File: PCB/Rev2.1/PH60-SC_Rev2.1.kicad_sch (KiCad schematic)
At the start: 44 parts, among them J1 USB_C_Receptacle_USB2.0_14P, J2 Conn_01x02_Pin, J3 Conn_01x02_Pin, U1 nRF52840, X1 32.768kHz, X2 Crystal_Generic

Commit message: 扇出sc7a210h开发用引脚
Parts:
- added J4: Conn_01x08_Pin, Connector_PinSocket_2.54mm:PinSocket_1x08_P2.54mm_Vertical, symbol Connector:Conn_01x08_Pin
- added J5: Conn_01x03_Pin, Connector_PinSocket_2.54mm:PinSocket_1x03_P2.54mm_Vertical, symbol Connector:Conn_01x03_Pin
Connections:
- net GND: now also J4.8 (Pin_8)
- net VDD_NRF: now also J5.3 (Pin_3)
- net INT2: now reaches U1.A14 (P1.15)
- net INT2: now also J4.6 (Pin_6)
- net INT1: now reaches U1.A16 (P1.13)
- net INT1: now also J4.5 (Pin_5)
- net CS: now reaches U1.A20 (P1.10)
- net CS: now also J4.1 (Pin_1)
- net SDO/SA0: now reaches U1.B15 (P1.14)
- net SDO/SA0: now also J4.4 (Pin_4)
- net SDA/SDO/SDI: now reaches U1.B17 (P1.12)
- net SDA/SDO/SDI: now also J4.3 (Pin_3)
- net SCL/SPC: now reaches U1.B19 (P1.11)
- net SCL/SPC: now also J4.2 (Pin_2)
- net GPIO_VDD_OUT: now reaches U1.B9 (AIN6/P0.30)
- net GPIO_VDD_OUT: now also J5.1 (Pin_1)
- new net IMU_VCC: J4.7 (Pin_7), J5.2 (Pin_2)
- no-connect marks 24 -> 17
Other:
- moved on the sheet: J2, J3

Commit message: 丝印添加
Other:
- moved on the sheet: J5
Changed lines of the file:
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@@
 	)
 	(label "VDD_NRF"
-		(at 300.99 175.26 0)
+		(at 295.91 182.88 0)
 		(effects
 			(font
@@
 	)
 	(label "IMU_VCC"
-		(at 300.99 172.72 0)
+		(at 295.91 180.34 0)
 		(effects
 			(font
@@
 	)
 	(label "GPIO_VDD_OUT"
-		(at 300.99 170.18 0)
+		(at 295.91 177.8 0)
 		(effects
 			(font
@@
 	(symbol
 		(lib_id "Connector:Conn_01x03_Pin")
-		(at 295.91 172.72 0)
+		(at 290.83 180.34 0)
 		(unit 1)
 		(body_style 1)
@@
 		(fields_autoplaced yes)
 		(property "Reference" "J5"
-			(at 296.545 165.1 0)
+			(at 291.465 172.72 0)
 			(show_name no)
 			(do_not_autoplace no)
@@
 		)
 		(property "Value" "Conn_01x03_Pin"
-			(at 296.545 167.64 0)
+			(at 291.465 175.26 0)
 			(show_name no)
 			(do_not_autoplace no)
@@
 		)
 		(property "Footprint" "Connector_PinSocket_2.54mm:PinSocket_1x03_P2.54mm_Vertical"
-			(at 295.91 172.72 0)
+			(at 290.83 180.34 0)
 			(hide yes)
 			(show_name no)
@@
 		)
 		(property "Datasheet" ""
-			(at 295.91 172.72 0)
+			(at 290.83 180.34 0)
 			(hide yes)
 			(show_name no)
@@
 		)
 		(property "Description" "Generic connector, single row, 01x03, script generated"
-			(at 295.91 172.72 0)
-			(hide yes)
-			(show_name no)
+			(at 290.83 180.34 0)
+			(hide yes)
+			(show_name no)

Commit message: 调整天线封装与相关外围元件bom，c27dnf，0欧电阻换1.2nh电感
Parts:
- removed R3: 0R, Capacitor_SMD:C_0402_1005Metric, symbol Device:R
- added L5: 1.2 nH, Inductor_SMD:L_0402_1005Metric, symbol Device:L_Small
- C10: value 0.5p -> 2.8p
- C27: now left out of the parts list
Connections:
- net at AE1.1 (A), C27.2: now also L5.1
- net at C10.2, L2.1: now also L5.2
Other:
- note added: "C27（DNF）"
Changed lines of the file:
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@@
 		)
 	)
+	(text "C27（DNF）"
+		(exclude_from_sim no)
+		(at 139.954 109.474 0)
+		(effects
+			(font
+				(size 1.27 1.27)
+			)
+		)
+	)
 	(text "ESD"
 		(exclude_from_sim no)
@@
 	(wire
 		(pts
+			(xy 158.75 104.14) (xy 163.83 104.14)
+		)
+		(stroke
+			(width 0)
+			(type default)
+		)
+	)
+	(wire
+		(pts
 			(xy 181.61 193.04) (xy 190.5 193.04)
 		)
@@
 	(wire
 		(pts
-			(xy 160.02 104.14) (xy 163.83 104.14)
-		)
-		(stroke
-			(width 0)
-			(type default)
-		)
-	)
-	(wire
-		(pts
 			(xy 275.59 60.96) (xy 285.75 60.96)
 		)
@@
 	(wire
 		(pts
-			(xy 147.32 104.14) (xy 152.4 104.14)
+			(xy 147.32 104.14) (xy 153.67 104.14)
 		)
 		(stroke
@@
 	)
 	(symbol
-		(lib_id "Device:R")
-		(at 156.21 104.14 90)
-		(unit 1)
-		(body_style 1)
-		(exclude_from_sim no)
-		(in_bom yes)
-		(on_board yes)
-		(in_pos_files yes)
-		(dnp no)
-		(fields_autoplaced yes)
-		(property "Reference" "R3"
-			(at 156.21 97.79 90)
-			(show_name no)
-			(do_not_autoplace no)
-			(effects
-				(font
-					(size 1.27 1.27)
-				)
-			)
-		)
-		(property "Value" "0R"
-			(at 156.21 100.33 90)
-			(show_name no)
-			(do_not_autoplace no)
-			(effects
-				(font
-					(size 1.27 1.27)
-				)
-			)
-		)
-		(property "Footprint" "Capacitor_SMD:C_0402_1005Metric"
-			(at 156.21 105.918 90)
-			(hide yes)
-			(show_name no)
-			(do_not_autoplace no)
-			(effects
-				(font
-					(size 1.27 1.27)
-				)
-			)
-		)
-		(property "Datasheet" ""
-			(at 156.21 104.14 0)
-			(hide yes)
-			(show_name no)
-			(do_not_autoplace no)
-			(effects
-				(font
-					(size 1.27 1.27)
-				)
-			)
-		)
-		(property "Description" "Resistor"
-			(at 156.21 104.14 0)
-			(hide yes)
-			(show_name no)
-			(do_not_autoplace no)
-			(effects
-				(font
-					(size 1.27 1.27)
-				)
-			)
-		)
-		(pin "2"
-		)
-		(pin "1"
-		)
-		(instances
-			(project "PH60-SC_Rev2.1"
-				(path "/dca0f898-8fdb-4522-a51d-f4f4238906e7"
-					(reference "R3")
-					(unit 1)
-				)
-			)
-		)
-	)
-	(symbol
 		(lib_id "Device:C_Small")
 		(at 139.7 54.61 0)
@@
 			)
 		)
-		(property "Value" "0.5p"
+		(property "Value" "2.8p"
 			(at 166.37 109.2135 0)
 			(show_name no)
@@
 		(body_style 1)
 		(exclude_from_sim no)
-		(in_bom yes)
+		(in_bom no)
 		(on_board yes)
 		(in_pos_files yes)
@@
 					(unit 1)
 				)
+			)
+		)
+	)
+	(symbol
+		(lib_id "Device:L_Small")
+		(at 156.21 104.14 90)
+		(unit 1)
+		(body_style 1)
+		(exclude_from_sim no)
+		(in_bom yes)
+		(on_board yes)
+		(in_pos_files yes)
+		(dnp no)
+		(fields_autoplaced yes)
+		(property "Reference" "L5"
+			(at 156.21 99.06 90)
+			(show_name no)
+			(do_not_autoplace no)
+			(effects
+				(font
+					(size 1.27 1.27)
+				)
+			)
+		)
+		(property "Value" "1.2 nH"
+			(at 156.21 101.6 90)
+			(show_name no)
+			(do_not_autoplace no)
+			(effects
+				(font
+					(size 1.27 1.27)
+				)
+			)
+		)
+		(property "Footprint" "Inductor_SMD:L_0402_1005Metric"
+			(at 156.21 104.14 0)
+			(hide yes)
+			(show_name no)
+			(do_not_autoplace no)
+			(effects
+				(font
+					(size 1.27 1.27)
+				)
+			)
+		)
+		(property "Datasheet" ""
+			(at 156.21 104.14 0)
+			(hide yes)
+			(show_name no)
+			(do_not_autoplace no)
+			(effects
+				(font
+					(size 1.27 1.27)
+				)
+			)
+		)
+		(property "Description" "Inductor, small symbol"
+			(at 156.21 104.14 0)
+			(hide yes)
+			(show_name no)
+			(do_not_autoplace no)
+			(effects
+				(font
+					(size 1.27 1.27)
+				)
+			)
+		)
+		(pin "2"
+		)
+		(pin "1"
+		)
+		(instances
+			(project "PH60-SC_Rev2.1"
+				(path "/dca0f898-8fdb-4522-a51d-f4f4238906e7"
+					(reference "L5")
+					(unit 1)
+				)

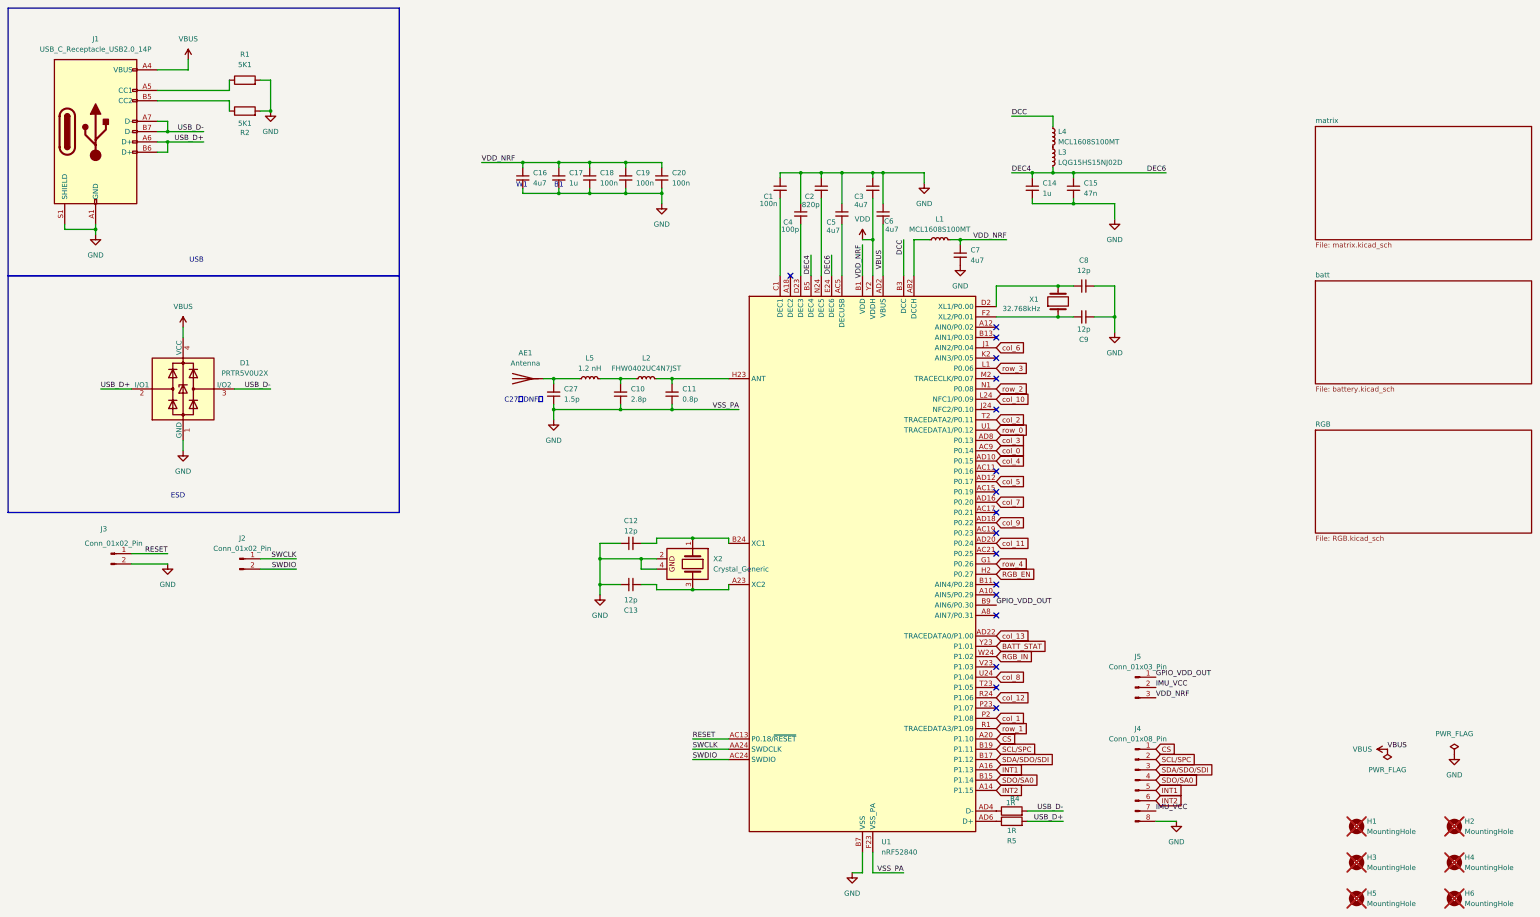
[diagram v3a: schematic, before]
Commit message: 布局调整，rgb，轴座调整，注意二极管位置为手动校准
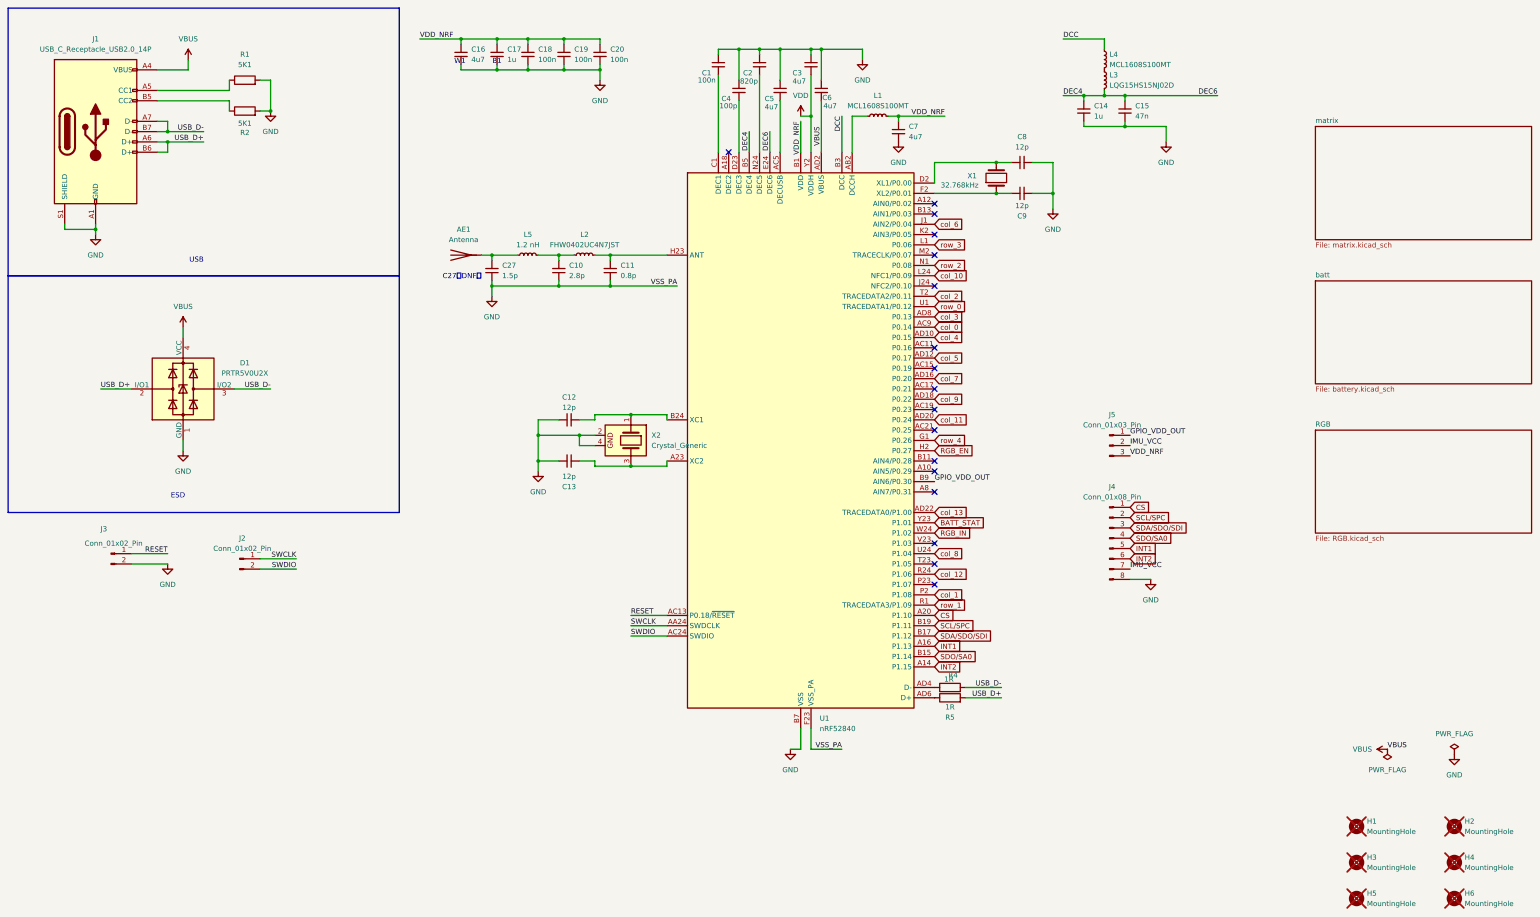
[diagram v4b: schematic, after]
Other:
- moved on the sheet: AE1, C1, C10, C11, C12, C13, C14, C15, C16, C17, C18, C19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

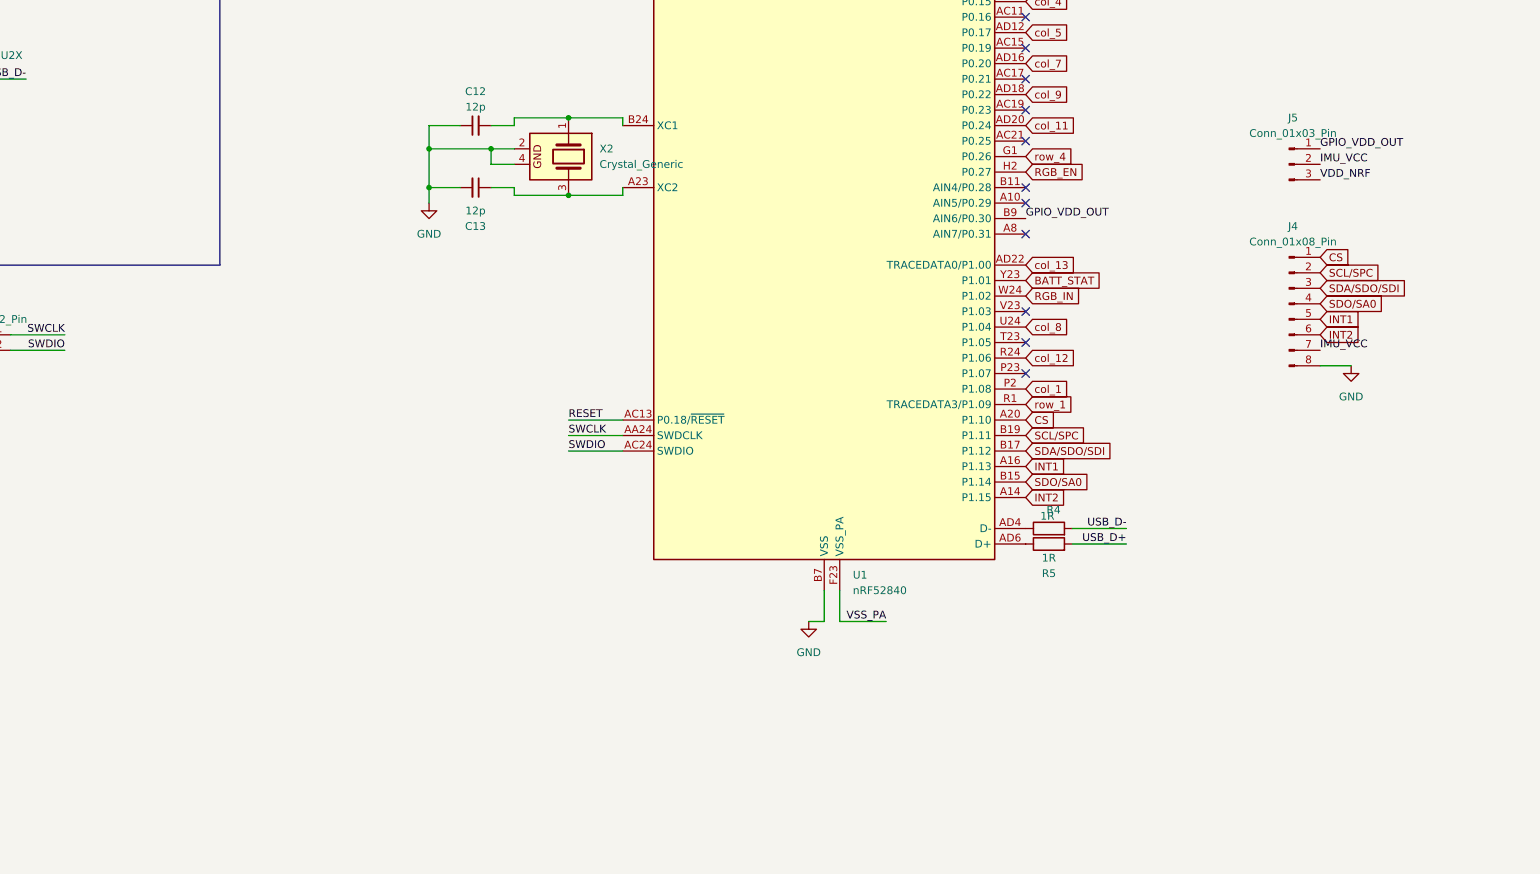
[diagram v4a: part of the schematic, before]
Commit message: 原理图添加LIS2DH12
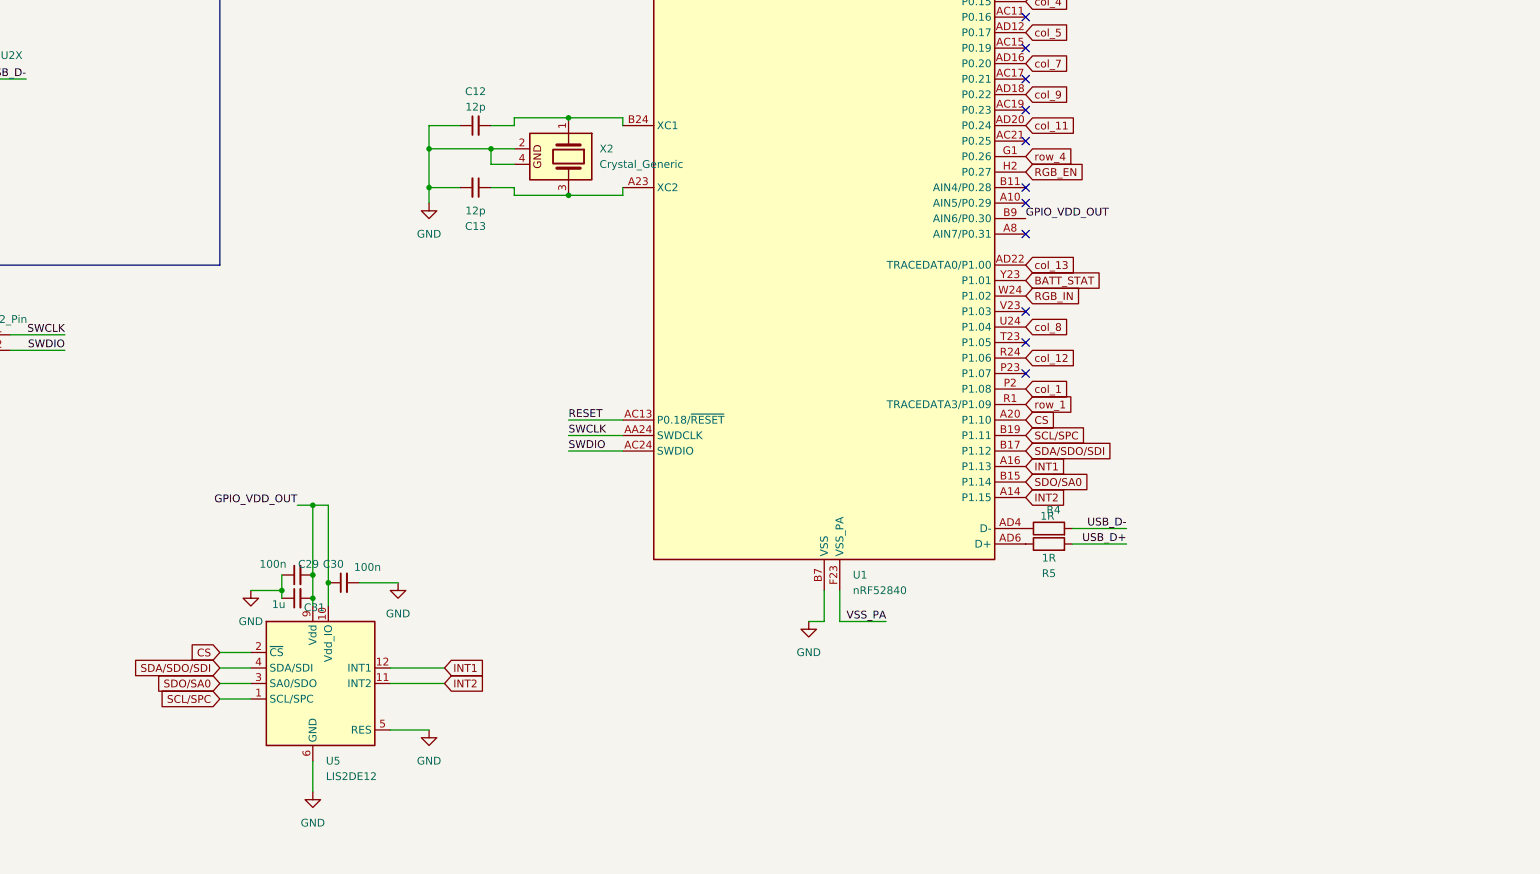
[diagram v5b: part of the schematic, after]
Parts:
- removed J4: Conn_01x08_Pin, Connector_PinSocket_2.54mm:PinSocket_1x08_P2.54mm_Vertical, symbol Connector:Conn_01x08_Pin
- removed J5: Conn_01x03_Pin, Connector_PinSocket_2.54mm:PinSocket_1x03_P2.54mm_Vertical, symbol Connector:Conn_01x03_Pin
- added C29, C30: 100n, Capacitor_SMD:C_0402_1005Metric, symbol Device:C_Small
- added C31: 1u, Capacitor_SMD:C_0402_1005Metric, symbol Device:C_Small
- added U5: LIS2DE12, Package_LGA:LGA-12_2x2mm_P0.5mm, symbol Sensor_Motion:LIS2DE12
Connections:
- net CS: now also U5.2 (~{CS})
- net GND: now also C29.1, C30.2, C31.1, U5.5 (RES), U5.6 (GND), U5.7 (GND), U5.8 (GND)
- net GPIO_VDD_OUT: now also C29.2, C30.1, C31.2, U5.10 (Vdd_IO), U5.9 (Vdd)
- net INT1: now also U5.12 (INT1)
- net INT2: now also U5.11 (INT2)
- net SCL/SPC: now also U5.1 (SCL/SPC)
- net SDA/SDO/SDI: now also U5.4 (SDA/SDI)
- net SDO/SA0: now also U5.3 (SA0/SDO)

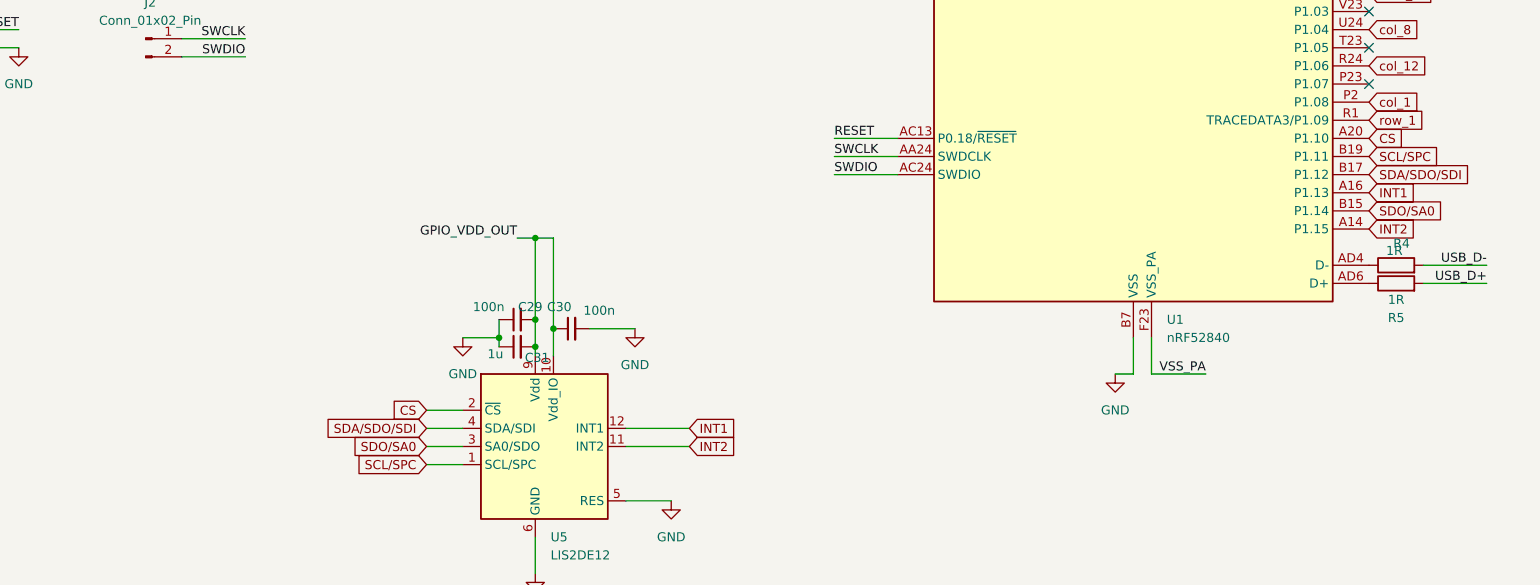
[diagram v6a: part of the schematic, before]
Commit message: imu原理图调整并优化布局
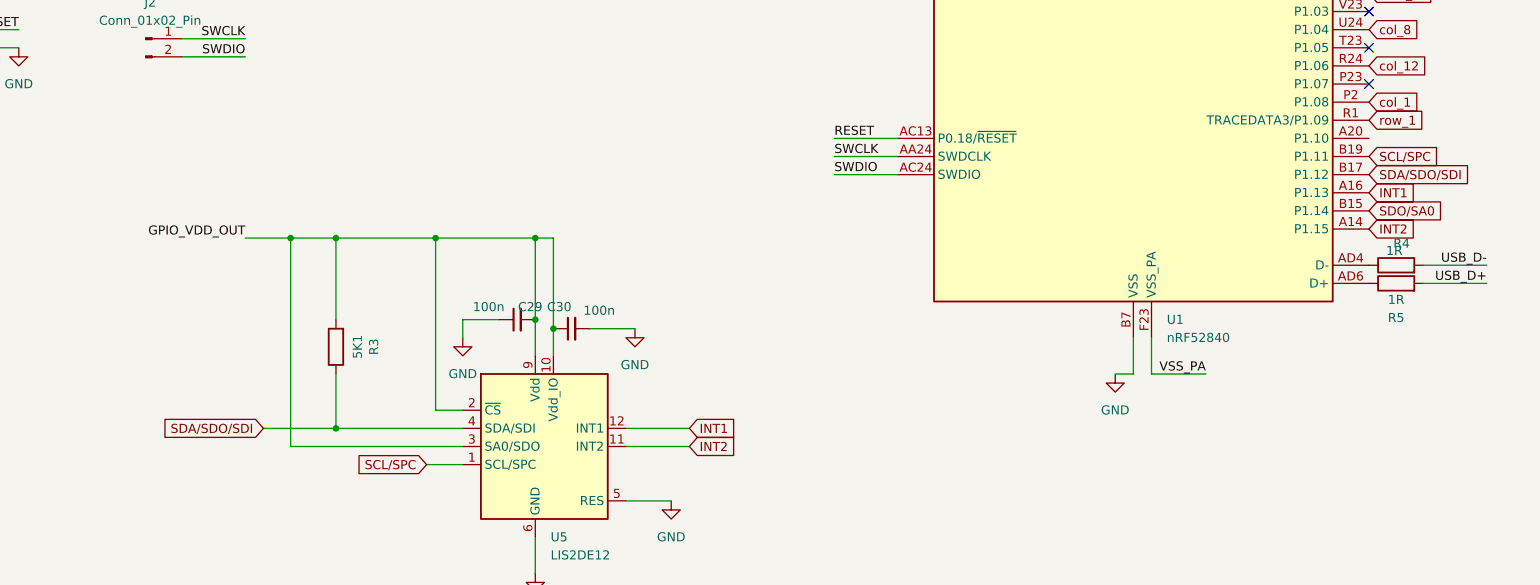
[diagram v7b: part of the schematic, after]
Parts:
- removed C31: 1u, Capacitor_SMD:C_0402_1005Metric, symbol Device:C_Small
- added R3: 5K1, Resistor_SMD:R_0402_1005Metric, symbol Device:R
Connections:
- net GPIO_VDD_OUT: now also U5.2 (~{CS}), U5.3 (SA0/SDO), R3.2
- net SDA/SDO/SDI: now also R3.1
- net SDO/SA0: no longer U5.3 (SA0/SDO)
- net CS: no longer names the net of U1.A20 (P1.10)
- net CS: no longer U5.2 (~{CS})
